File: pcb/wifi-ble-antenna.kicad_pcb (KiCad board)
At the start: 2 copper layers, 0 parts

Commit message: PCB: Define stackup and pre-defined sizes, init PCB layout
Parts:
- added C1: C-0402-template, DW-footprints:C_0402_1005Metric, F.Cu at (130.1, 105.5)
- added C2: C-0402-template, DW-footprints:C_0402_1005Metric, F.Cu at (133.1, 105.5)
- added E1: IFA_2.4GHz, DW-footprints:Antenna_Custom_IFA_2.4GHz, F.Cu at (137.1, 101.1)
- added J1: BWSMA-KE-P001, DW-footprints:Conn_SMA_BWSMA-KE-P001, F.Cu at (122.2, 105.0)
- added R1: R-0R-0402, DW-footprints:R_0402_1005Metric, F.Cu at (128.6, 105.0)
- added R2: R-0R-0402, DW-footprints:R_0402_1005Metric, F.Cu at (131.6, 105.0)
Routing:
- net Net-(J1-Pad1): track 0.00 -> 5.85 mm
- net Net-(C1-Pad2): track 0.00 -> 2.00 mm
- net Net-(E1-SIG): track 0.00 -> 1.95 mm
- net GND: vias 0 -> 4
- added copper zone on In1.Cu, net GND
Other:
- board outline added: 30 x 30 mm
- copper layers 2 -> 4
- board text added: "PROJECT Rev. ${REVISION} BRD SHA: %%%%%%%% Date: ${CURRENT_DATE}"

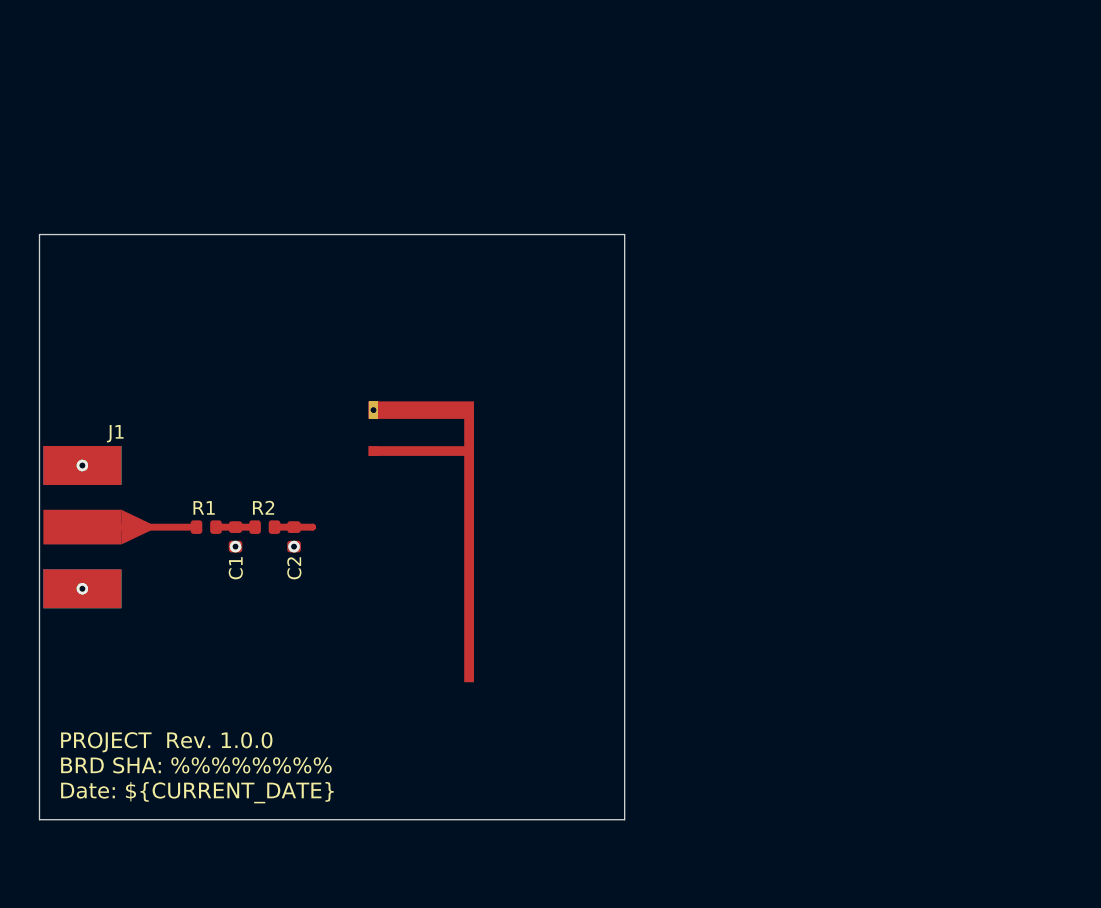
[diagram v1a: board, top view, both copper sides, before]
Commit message: PCB: Add IFA, initial layout
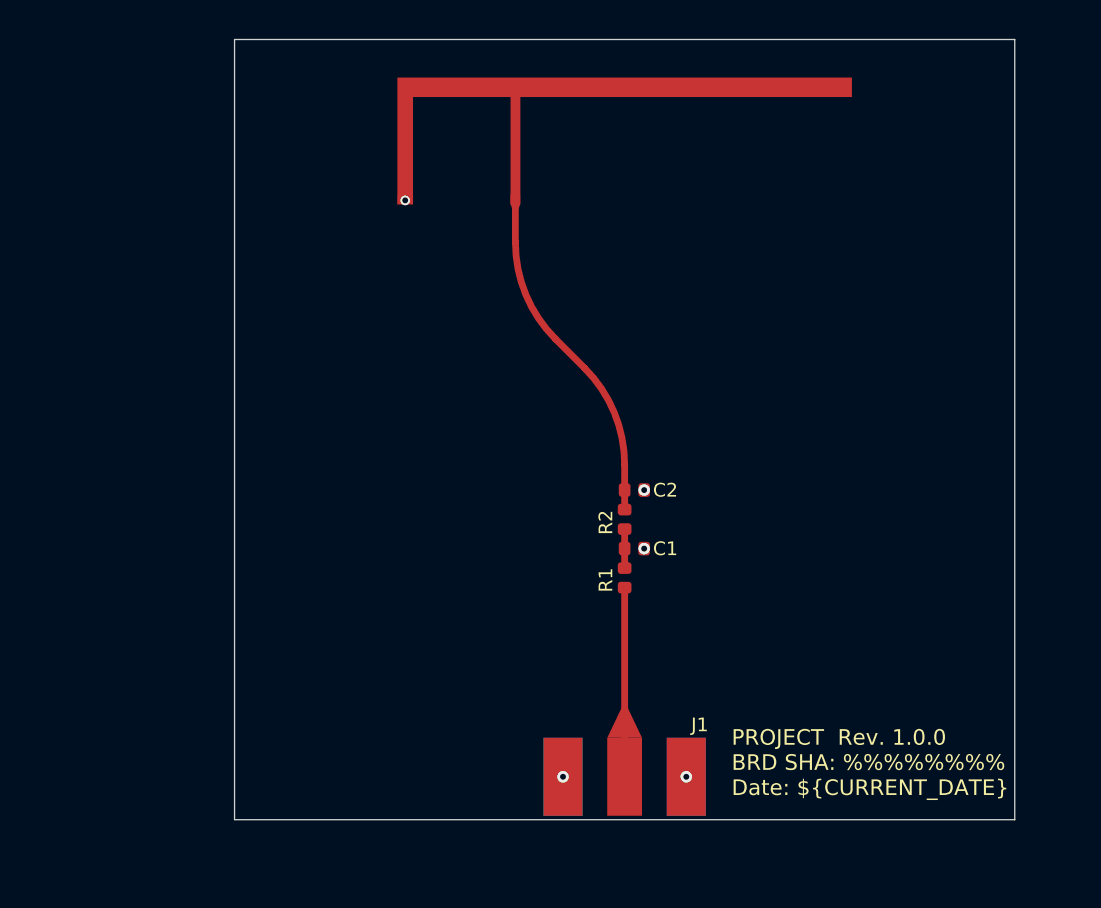
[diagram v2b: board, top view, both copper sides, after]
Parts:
- moved J1 30.6 mm to (150.0, 117.8), turned to 180 degrees
- moved R1 21.6 mm to (150.0, 107.6), turned to 90 degrees
- moved C1 20.5 mm to (150.5, 106.1), turned to 180 degrees
- moved R2 18.5 mm to (150.0, 104.6), turned to 90 degrees
- moved C2 17.6 mm to (150.5, 103.1), turned to 180 degrees
- moved E1 14.8 mm to (144.4, 88.2), turned to 0 degrees
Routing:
- net Net-(E1-SIG): track 1.95 -> 17.5 mm
- net Net-(J1-Pad1): track 5.85 -> 9.70 mm
- net GND: vias 4 -> 5
- added copper zone on In2.Cu, net GND
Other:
- board size 30 x 30 mm -> 40 x 40 mm

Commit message: PCB: Finalize layout - add impedance matching geometry to SMA, ensure dimensions are as designed
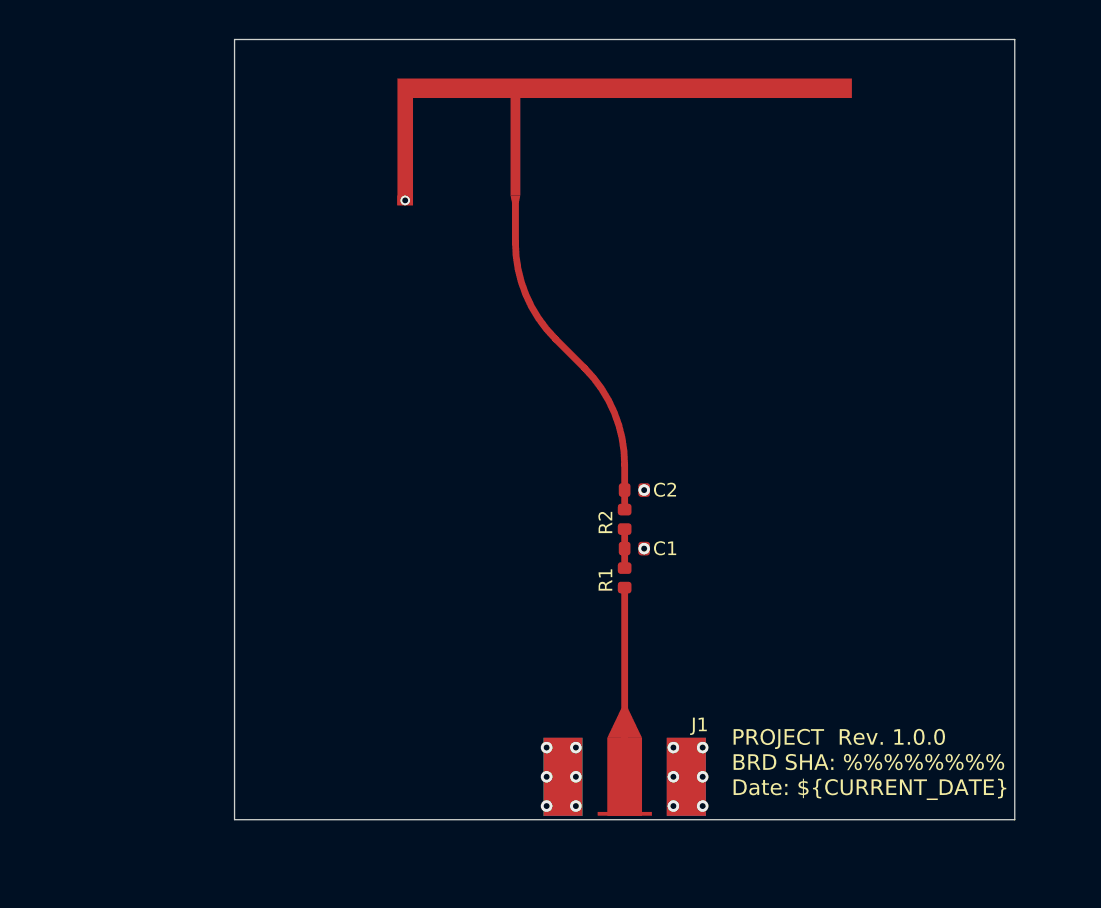
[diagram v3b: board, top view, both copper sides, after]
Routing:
- net GND: vias 5 -> 15

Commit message: PCB: Add stackup table, origin points, cleanup silkscreen, add via stitching
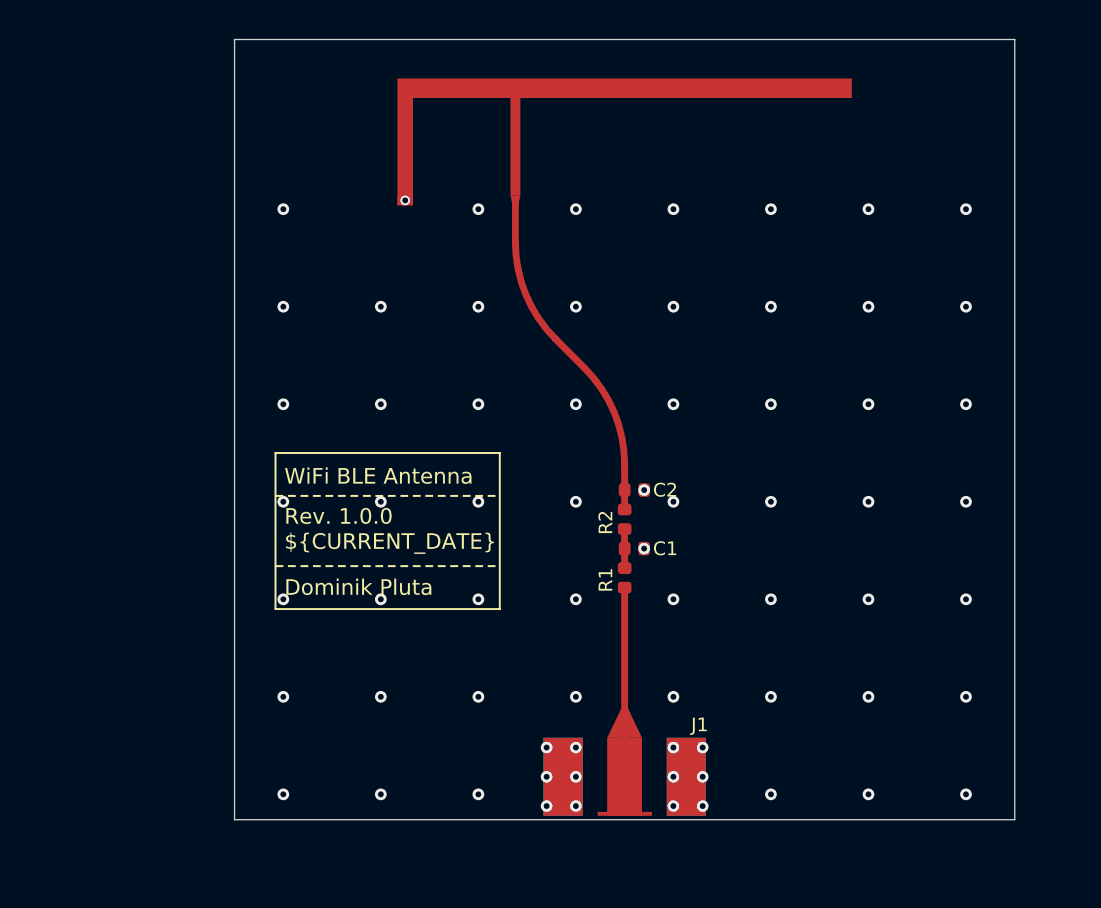
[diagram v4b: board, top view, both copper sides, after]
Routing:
- net GND: vias 15 -> 68
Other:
- board text added: "0"
- board text added: "0 mm"
- board text added: "0.01 mm"
- board text added: "0.0152 mm"
- board text added: "0.02"
- board text added: "0.035 mm"
- board text added: "0.2104 mm"
- board text added: "1"
- board text added: "1.065 mm"
- board text added: "3.3"
- board text added: "4.4"
- board text added: "4.6"
- board text added: "B.Cu"
- board text added: "B.Mask"
- board text added: "B.Paste"
- board text added: "B.Silkscreen"
- board text added: "Black"
- board text added: "Bottom Silk Screen"
- board text added: "Bottom Solder Mask"
- board text added: "Bottom Solder Paste"
- board text added: "Color"
- board text added: "Dielectric"
- board text added: "Dominik Pluta"
- board text added: "Epsilon R"
- board text added: "F.Cu"
- board text added: "F.Mask"
- board text added: "F.Paste"
- board text added: "F.Silkscreen"
- board text added: "FR4"
- board text added: "FR4 natural"
- board text added: "In1.Cu"
- board text added: "In2.Cu"
- board text added: "Layer Name"
- board text added: "Loss Tangent"
- board text added: "Material"
- board text added: "Not specified"
- board text added: "Rev. ${REVISION} ${CURRENT_DATE}"
- board text added: "SHA: %%%%%%%%"
- board text added: "Thickness (mm)"
- board text added: "Top Silk Screen"
- board text added: "Top Solder Mask"
- board text added: "Top Solder Paste"
- board text added: "Type"
- board text added: "White"
- board text added: "WiFi BLE Antenna"
- board text added: "copper"
- board text added: "core"
- board text added: "prepreg"
- board text removed: "PROJECT Rev. ${REVISION} BRD SHA: %%%%%%%% Date: ${CURRENT_DATE}"

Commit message: PCB: Match PCB dimensions exactly with the simulations
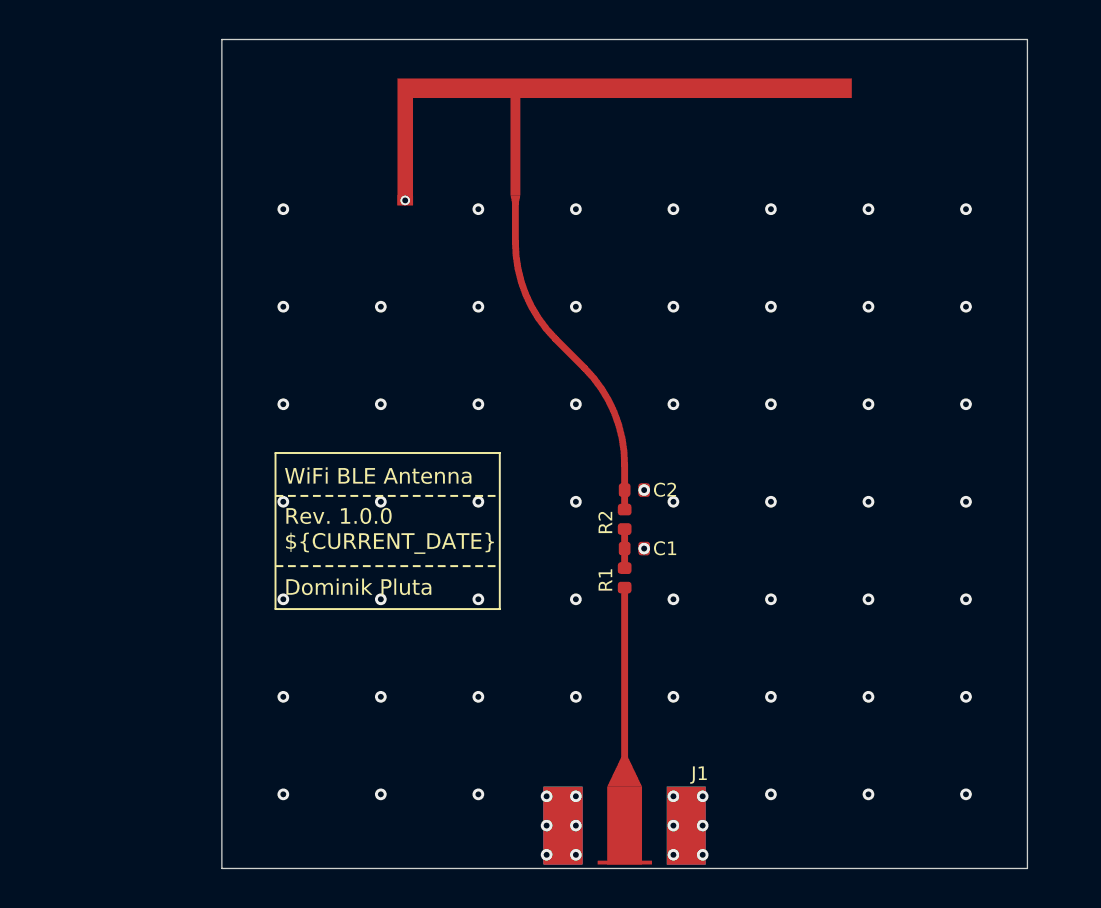
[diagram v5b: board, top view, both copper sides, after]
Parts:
- moved J1 2.50 mm to (150.0, 120.3)
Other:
- board size 40 x 40 mm -> 41.3 x 42.5 mm
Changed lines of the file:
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@@
 		(allow_soldermask_bridges_in_footprints no)
 		(tenting front back)
-		(aux_axis_origin 130 120)
-		(grid_origin 130 120)
+		(aux_axis_origin 129.35 122.5)
+		(grid_origin 129.35 122.5)
 		(pcbplotparams
 			(layerselection 0x00000000_00000000_55555555_5755f5ff)
@@
 	(footprint "DW-footprints:Conn_SMA_BWSMA-KE-P001"
 		(layer "F.Cu")
-		(at 150 117.8 180)
+		(at 150 120.3 180)
 		(descr "SMA connector, SMD")
 		(tags "CONNECTOR")
@@
 	(gr_poly
 		(pts
-			(xy 149.825376 114.300001) (xy 149.110001 115.8) (xy 150.890001 115.8) (xy 150.174626 114.300001)
+			(xy 149.825376 116.800001) (xy 149.110001 118.3) (xy 150.890001 118.3) (xy 150.174626 116.800001)
 		)
 		(stroke
@@
 	(gr_poly
 		(pts
-			(xy 148.618398 119.6) (xy 148.618398 119.8) (xy 151.398398 119.8) (xy 151.398398 119.6)
+			(xy 148.618398 122.1) (xy 148.618398 122.3) (xy 151.398398 122.3) (xy 151.398398 122.1)
 		)
 		(stroke
@@
 	)
 	(gr_rect
-		(start 130 80)
-		(end 170 120)
+		(start 129.35 80)
+		(end 170.65 122.5)
 		(stroke
 			(width 0.05)
@@
 	)
 	(gr_text "SHA: %%%%%%%%"
-		(at 131 119 0)
+		(at 131 121.5 0)
 		(layer "B.SilkS")
 		(effects
@@
 	)
 	(via
-		(at 152.5 117.8)
+		(at 152.5 120.3)
 		(size 0.6)
 		(drill 0.3)
@@
 	)
 	(via
-		(at 146 119.3)
+		(at 146 121.8)
 		(size 0.6)
 		(drill 0.3)
@@
 	)
 	(via
-		(at 154 116.3)
+		(at 154 118.8)
 		(size 0.6)
 		(drill 0.3)
@@
 	)
 	(via
-		(at 152.5 116.3)
+		(at 152.5 118.8)
 		(size 0.6)
 		(drill 0.3)
@@
 	)
 	(via
-		(at 146 116.3)
+		(at 146 118.8)
 		(size 0.6)
 		(drill 0.3)
@@
 	)
 	(via
-		(at 154 117.8)
+		(at 154 120.3)
 		(size 0.6)
 		(drill 0.3)
@@
 	)
 	(via
-		(at 146 117.8)
+		(at 146 120.3)
 		(size 0.6)
 		(drill 0.3)
@@
 	)
 	(via
-		(at 154 119.3)
+		(at 154 121.8)
 		(size 0.6)
 		(drill 0.3)
@@
 	)
 	(via
-		(at 147.5 119.3)
+		(at 147.5 121.8)
 		(size 0.6)
 		(drill 0.3)
@@
 	)
 	(via
-		(at 152.5 119.3)
+		(at 152.5 121.8)
 		(size 0.6)
 		(drill 0.3)
@@
 	)
 	(via
-		(at 147.5 116.3)
+		(at 147.5 118.8)
 		(size 0.6)
 		(drill 0.3)
@@
 	)
 	(via
-		(at 147.5 117.8)
+		(at 147.5 120.3)
 		(size 0.6)
 		(drill 0.3)
@@
 	)
 	(segment
-		(start 150.000001 117.8)
-		(end 150 117.799999)
+		(start 150.000001 120.3)
+		(end 150 120.299999)
 		(width 0.3493)
 		(layer "F.Cu")
@@
 			(thermal_gap 0.5)
 			(thermal_bridge_width 0.5)
+			(smoothing fillet)
+			(radius 0.1)
 		)
 		(polygon
 			(pts
-				(xy 170 120) (xy 170 87.999999) (xy 130 87.999999) (xy 130 120)
+				(xy 145.65 122) (xy 145.65 122.3) (xy 154.35 122.3) (xy 154.35 122) (xy 170.15 122) (xy 170.15 87.999999)
+				(xy 129.85 87.999999) (xy 129.85 122)
 			)
 		)
@@
 		(polygon
 			(pts
-				(xy 150 114.300001) (xy 151.275 115.800001) (xy 151.275 120.000001) (xy 148.725 120.000001) (xy 148.725 115.800001)
+				(xy 150 116.800001) (xy 151.275 118.300001) (xy 151.275 122.500001) (xy 148.725 122.500001) (xy 148.725 118.300001)
 			)
 		)
